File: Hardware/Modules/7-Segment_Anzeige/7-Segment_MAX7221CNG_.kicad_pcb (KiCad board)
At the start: 2 copper layers, 77 x 77 mm, 9 parts, among them J2 B6B-EH-A, U1 MAX7221xNG, U4 CC56-12SURKWA, U5 CC56-12SURKWA

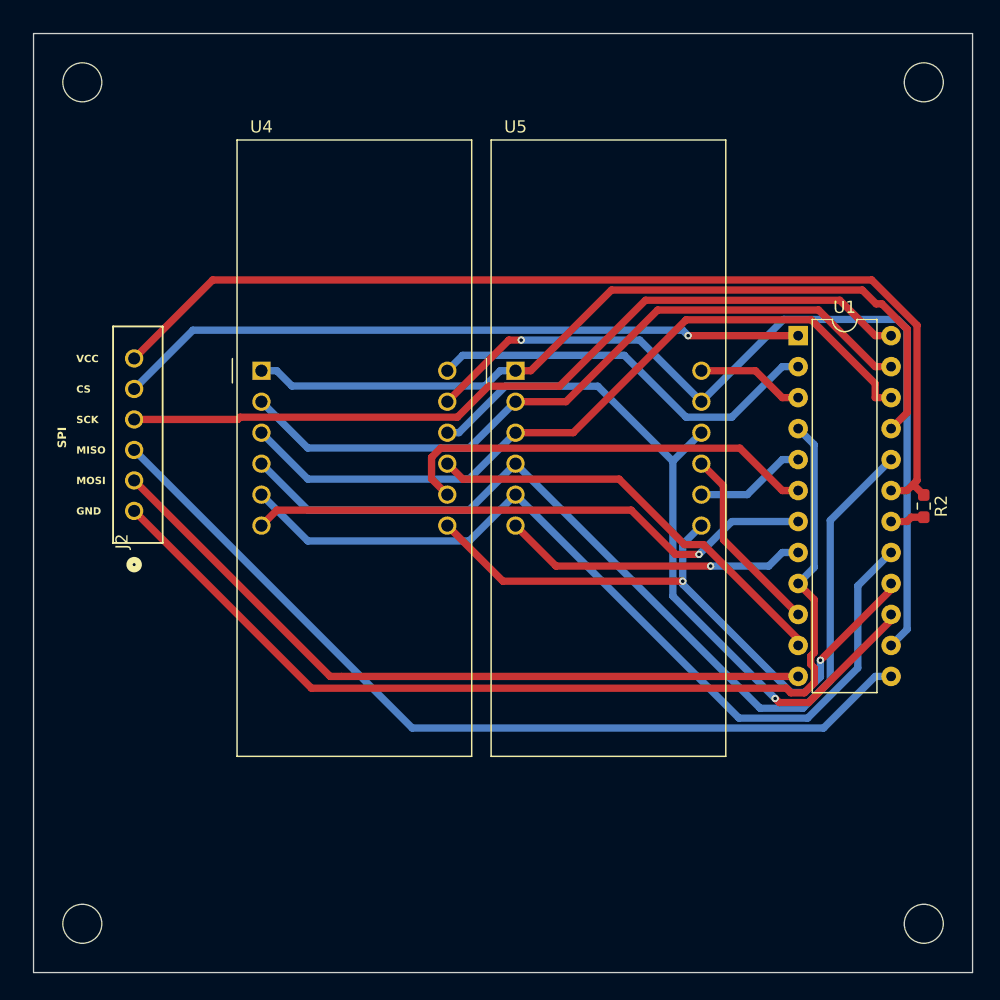
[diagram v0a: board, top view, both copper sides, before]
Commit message: fixed connector orientation
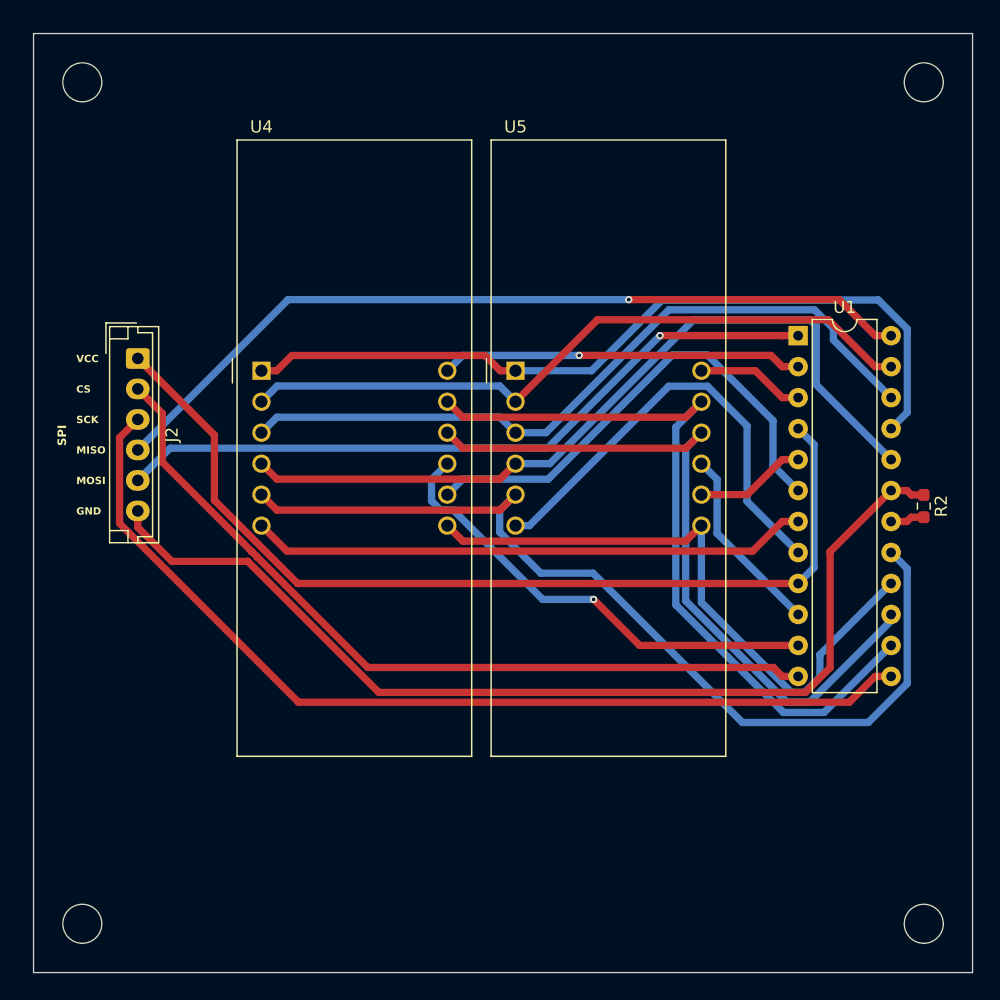
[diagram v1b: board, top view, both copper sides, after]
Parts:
- J2: footprint Connector:CONN_B6B-EH-A_JST -> Connector_JST:JST_EH_B6B-EH-A_1x06_P2.50mm_Vertical
- moved J2 12.5 mm to (39.3, 59.4), turned to -90 degrees
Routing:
- net Net-(U1-SEG_C): track 79.3 -> 65.2 mm
- net Net-(U1-DIG_7): track 25.0 -> 37.2 mm, vias 1 -> 0
- net Net-(U1-SEG_A): track 71.5 -> 63.0 mm, vias 1 -> 0
- net Net-(J2-Pad1): track 85.0 -> 78.7 mm
- net Net-(U1-CLK): track 73.3 -> 79.4 mm
- net Net-(U1-SEG_G): track 71.9 -> 78.0 mm
- net Net-(U1-~{CS}): track 61.1 -> 66.3 mm
- net Net-(U1-DIG_2): track 35.4 -> 40.3 mm
- net Net-(U1-DIG_0): track 33.1 -> 29.7 mm, vias 0 -> 1
- net Net-(U1-DIG_1): track 35.2 -> 38.6 mm, vias 0 -> 1
- net Net-(U1-SEG_D): track 59.8 -> 57.1 mm
- net Net-(U1-DIN): track 56.6 -> 59.1 mm
- net Net-(U1-SEG_F): track 61.8 -> 59.8 mm, vias 1 -> 0
- net Net-(U1-SEG_DP): track 61.9 -> 60.4 mm
- net Net-(U1-DIG_3): track 47.2 -> 45.9 mm, vias 1 -> 0
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
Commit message: fixed GND/VCC issue and added filling zone
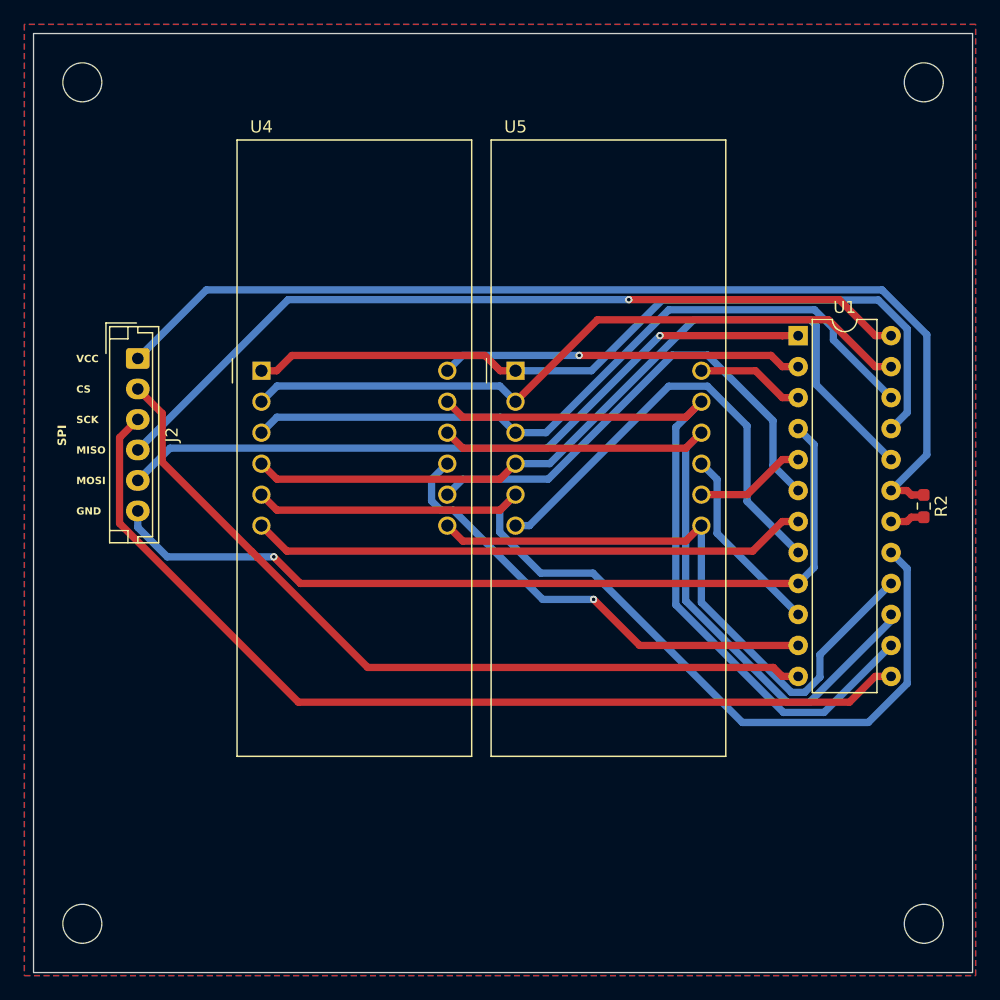
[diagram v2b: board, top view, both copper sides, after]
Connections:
- J2 pad 1: Net-(J2-Pad1) -> Net-(U1-V+)
- J2 pad 6: Net-(U1-V+) -> Net-(J2-Pad6)
- U1 pad 4: Net-(J2-Pad1) -> Net-(J2-Pad6)
- U1 pad 9: Net-(J2-Pad1) -> Net-(J2-Pad6)
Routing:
- net Net-(J2-Pad1): track 78.7 -> 0.00 mm
- net Net-(J2-Pad6): track 0.00 -> 71.2 mm, vias 0 -> 1
- net Net-(U1-V+): track 84.0 -> 85.4 mm
- added copper zone on B.Cu, net Net-(J2-Pad6)
- added copper zone on F.Cu, net Net-(J2-Pad6)

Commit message: Added capacitors to 7-segment display
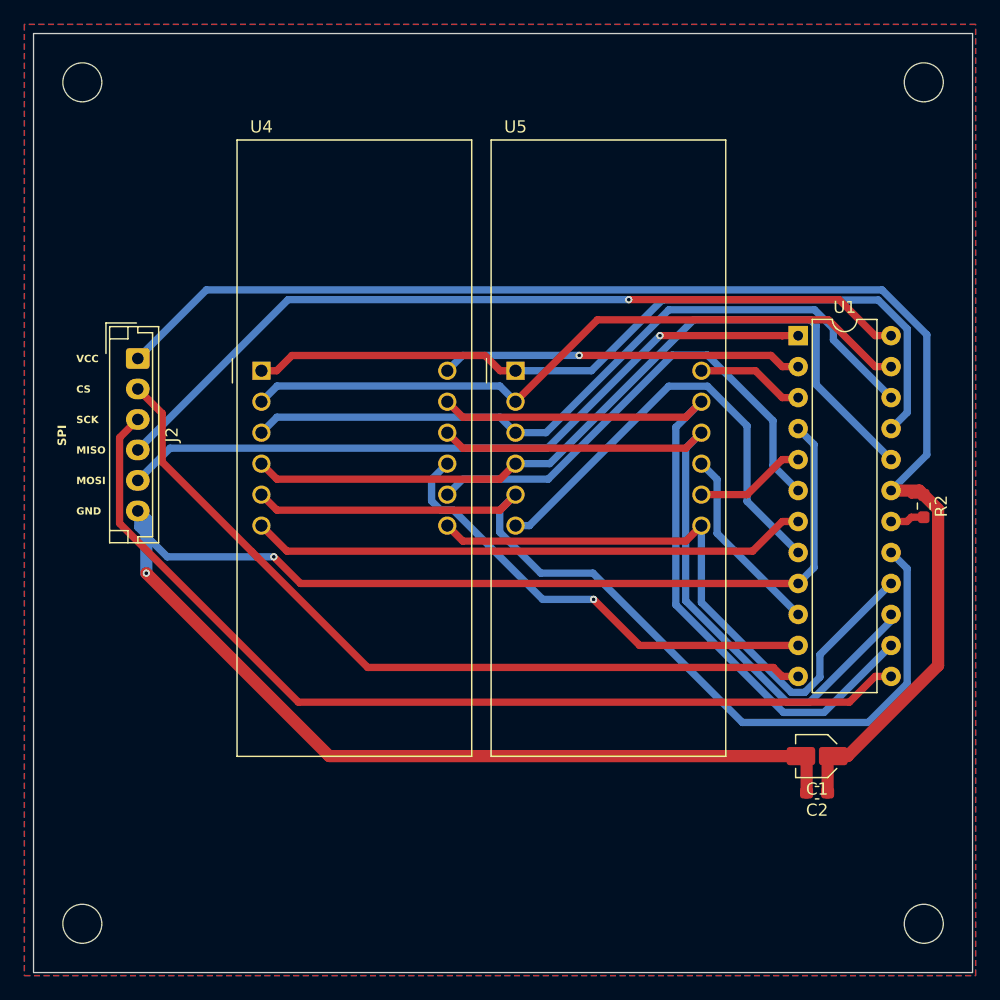
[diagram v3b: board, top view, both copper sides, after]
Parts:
- added C1: 10µF, Capacitor_SMD:C_Elec_3x5.4, F.Cu at (95.0, 92.0)
- added C2: 0.1µF, Capacitor_SMD:C_0603_1608Metric_Pad1.08x0.95mm_HandSolder, F.Cu at (95.0, 95.0)
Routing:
- net Net-(C1-Pad2): track 71.2 -> 139.7 mm, vias 1 -> 2
- net Net-(U1-V+): track 85.4 -> 117.5 mm
